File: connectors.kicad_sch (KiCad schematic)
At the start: 6 parts, among them J1 Conn_01x02, J2 Conn_01x02, J3 Conn_01x04, J4 Conn_01x04, J5 USB_C_Receptacle_USB2.0, J6 Conn_PIC_ICSP_ICD

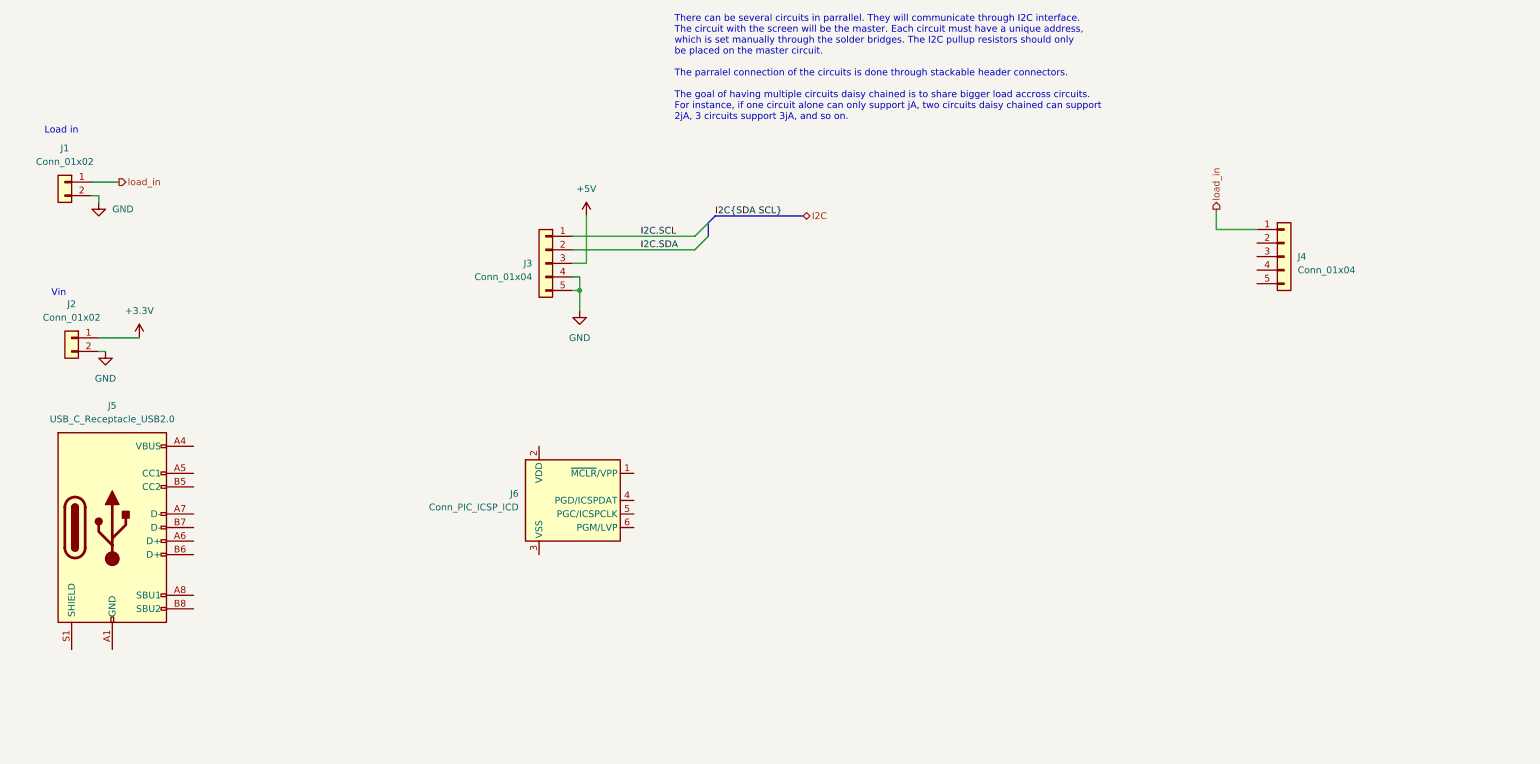
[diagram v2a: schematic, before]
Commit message: Add uart usb controller
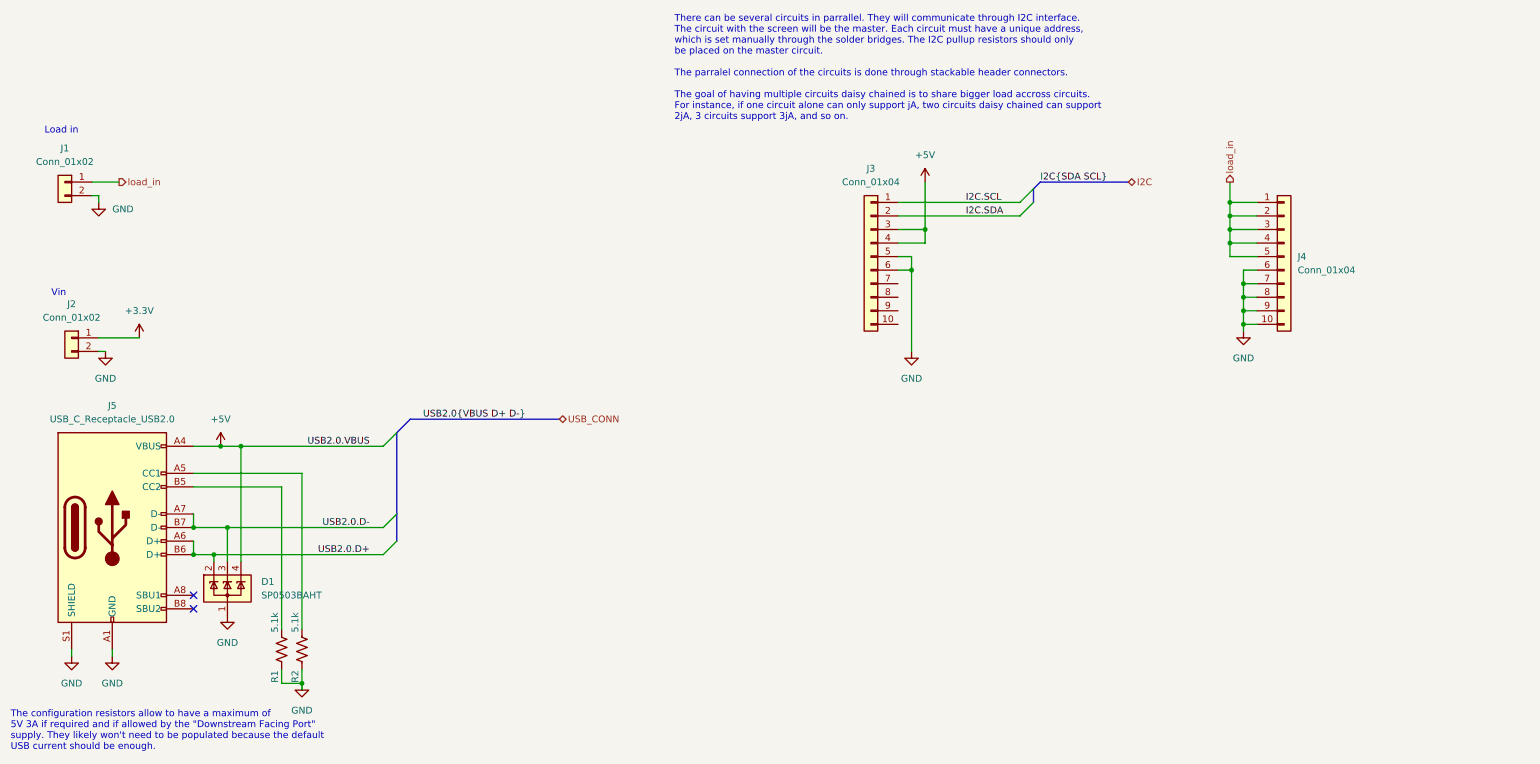
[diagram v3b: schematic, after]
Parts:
- removed J6: Conn_PIC_ICSP_ICD, Connector_PinHeader_2.54mm:PinHeader_1x06_P2.54mm_Vertical, symbol Connector:Conn_PIC_ICSP_ICD
- added D1: SP0503BAHT, Package_TO_SOT_SMD:SOT-143, symbol Power_Protection:SP0503BAHT
- added R1, R2: 5.1k, Resistor_SMD:R_0805_2012Metric, symbol Device:R_US
- J3, J4: footprint Connector_PinHeader_2.54mm:PinHeader_1x04_P2.54mm_Horizontal -> Connector_PinSocket_2.54mm:PinSocket_1x10_P2.54mm_Vertical; symbol Connector_Generic:Conn_01x05 -> Connector_Generic:Conn_01x10
- J5: footprint Connector_USB:USB_C_Plug_Molex_105444 -> Connector_USB:USB_C_Receptacle_GCT_USB4085
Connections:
- net +5V: now also J3.4 (Pin_4), J5.A4 (VBUS), J5.A9 (VBUS), J5.B4 (VBUS), J5.B9 (VBUS), D1.4 (K)
- net GND: now also J3.6 (Pin_6), J4.10 (Pin_10), J4.6 (Pin_6), J4.7 (Pin_7), J4.8 (Pin_8), J4.9 (Pin_9), J5.A1 (GND), J5.A12 (GND), J5.B1 (GND), J5.B12 (GND), J5.S1 (SHIELD), D1.1 (A), R1.1, R2.1; no longer J3.4 (Pin_4)
- net load_in: now also J4.2 (Pin_2), J4.3 (Pin_3), J4.4 (Pin_4), J4.5 (Pin_5)
- net at J5.A5 (CC1): now also R2.2
- net USB2.0.D+: now reaches J5.A6 (D+)
- net USB2.0.D+: now also J5.B6 (D+), D1.2 (K)
- net USB2.0.D-: now reaches J5.A7 (D-)
- net USB2.0.D-: now also J5.B7 (D-), D1.3 (K)
- net at J5.B5 (CC2): now also R1.2
- no-connect marks 0 -> 2
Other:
- note added: "The configuration resistors allow to have a maximum of 5V 3A if required and if allowed by the "Downstream Facing Port" supply. They likely won't need to be populated because the default USB current should be enough."

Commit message: WIP PCB Routing
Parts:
- removed J2: Conn_01x02, Connector_PinHeader_2.54mm:PinHeader_1x02_P2.54mm_Horizontal, symbol Connector_Generic:Conn_01x02
- D1: value SP0503BAHT -> (none); footprint Package_TO_SOT_SMD:SOT-143 -> (none)
- J1: value Conn_01x02 -> (none); footprint Connector_PinHeader_2.54mm:PinHeader_1x02_P2.54mm_Horizontal -> (none)
- J3, J4: value Conn_01x04 -> (none); footprint Connector_PinSocket_2.54mm:PinSocket_1x10_P2.54mm_Vertical -> (none)
- J5: value USB_C_Receptacle_USB2.0 -> (none); footprint Connector_USB:USB_C_Receptacle_GCT_USB4085 -> (none)
- R1, R2: value 5.1k -> (none); footprint Resistor_SMD:R_0805_2012Metric -> (none)
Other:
- note removed: "Vin"
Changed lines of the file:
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@@
-    (stroke (width 0) (type default) (color 0 0 0 0))
-  )
-  (wire (pts (xy 43.18 77.47) (xy 50.8 77.47))
     (stroke (width 0) (type default) (color 0 0 0 0))
   )
@@
   )
   (wire (pts (xy 60.96 113.03) (xy 67.31 113.03))
-    (stroke (width 0) (type default) (color 0 0 0 0))
-  )
-  (wire (pts (xy 43.18 80.01) (xy 44.45 80.01))
     (stroke (width 0) (type default) (color 0 0 0 0))
   )
@@
     (effects (font (size 1.27 1.27)) (justify left bottom))
   )
-  (text "Vin" (at 34.29 69.85 0)
-    (effects (font (size 1.27 1.27)) (justify left bottom))
-  )
   (text "There can be several circuits in parrallel. They will communicate through I2C interface.\nThe circuit with the screen will be the master. Each circuit must have a unique address, \nwhich is set manually through the solder bridges. The I2C pullup resistors should only \nbe placed on the master circuit.\n\nThe parralel connection of the circuits is done through stackable header connectors.\n\nThe goal of having multiple circuits daisy chained is to share bigger load accross circuits.\nFor instance, if one circuit alone can only support jA, two circuits daisy chained can support \n2jA, 3 circuits support 3jA, and so on."
     (at 151.13 36.83 0)
@@
     (in_bom yes) (on_board yes) (fields_autoplaced)
     (property "Reference" "J3" (id 0) (at 187.96 45.72 0))
-    (property "Value" "Conn_01x04" (id 1) (at 187.96 48.26 0))
-    (property "Footprint" "Connector_PinSocket_2.54mm:PinSocket_1x10_P2.54mm_Vertical" (id 2) (at 187.96 62.23 0)
+    (property "Value" "" (id 1) (at 187.96 48.26 0))
+    (property "Footprint" "" (id 2) (at 187.96 62.23 0)
       (effects (font (size 1.27 1.27)) hide)
     )
@@
     (pin "1")
   )
-  (symbol (lib_id "power:GND") (at 44.45 80.01 0) (unit 1)
-    (in_bom yes) (on_board yes) (fields_autoplaced)
-    (property "Reference" "#PWR0101" (id 0) (at 44.45 86.36 0)
-      (effects (font (size 1.27 1.27)) hide)
-    )
-    (property "Value" "GND" (id 1) (at 44.45 85.09 0))
-    (property "Footprint" "" (id 2) (at 44.45 80.01 0)
-      (effects (font (size 1.27 1.27)) hide)
-    )
-    (property "Datasheet" "" (id 3) (at 44.45 80.01 0)
-      (effects (font (size 1.27 1.27)) hide)
-    )
-    (pin "1")
-  )
   (symbol (lib_id "Device:R_US") (at 77.47 135.89 180) (unit 1)
     (in_bom no) (on_board yes)
     (property "Reference" "R1" (id 0) (at 76.2 140.97 90))
-    (property "Value" "5.1k" (id 1) (at 76.2 130.81 90))
-    (property "Footprint" "Resistor_SMD:R_0805_2012Metric" (id 2) (at 76.454 135.636 90)
+    (property "Value" "" (id 1) (at 76.2 130.81 90))
+    (property "Footprint" "" (id 2) (at 76.454 135.636 90)
       (effects (font (size 1.27 1.27)) hide)
     )
@@
     (in_bom yes) (on_board yes) (fields_autoplaced)
     (property "Reference" "J1" (id 0) (at 36.83 41.91 0))
-    (property "Value" "Conn_01x02" (id 1) (at 36.83 44.45 0))
-    (property "Footprint" "Connector_PinHeader_2.54mm:PinHeader_1x02_P2.54mm_Horizontal" (id 2) (at 36.83 48.26 0)
+    (property "Value" "" (id 1) (at 36.83 44.45 0))
+    (property "Footprint" "" (id 2) (at 36.83 48.26 0)
       (effects (font (size 1.27 1.27)) hide)
     )
@@
     (in_bom no) (on_board yes)
     (property "Reference" "R2" (id 0) (at 80.01 140.97 90))
-    (property "Value" "5.1k" (id 1) (at 80.01 130.81 90))
-    (property "Footprint" "Resistor_SMD:R_0805_2012Metric" (id 2) (at 80.264 135.636 90)
+    (property "Value" "" (id 1) (at 80.01 130.81 90))
+    (property "Footprint" "" (id 2) (at 80.264 135.636 90)
       (effects (font (size 1.27 1.27)) hide)
     )
@@
     (pin "1")
   )
-  (symbol (lib_id "Connector_Generic:Conn_01x02") (at 38.1 77.47 0) (mirror y) (unit 1)
-    (in_bom yes) (on_board yes) (fields_autoplaced)
-    (property "Reference" "J2" (id 0) (at 38.1 71.12 0))
-    (property "Value" "Conn_01x02" (id 1) (at 38.1 73.66 0))
-    (property "Footprint" "Connector_PinHeader_2.54mm:PinHeader_1x02_P2.54mm_Horizontal" (id 2) (at 38.1 77.47 0)
-      (effects (font (size 1.27 1.27)) hide)
-    )
-    (property "Datasheet" "~" (id 3) (at 38.1 77.47 0)
-      (effects (font (size 1.27 1.27)) hide)
-    )
-    (pin "1")
-    (pin "2")
-  )
-  (symbol (lib_id "power:+3.3V") (at 50.8 77.47 0) (unit 1)
-    (in_bom yes) (on_board yes) (fields_autoplaced)
-    (property "Reference" "#PWR0102" (id 0) (at 50.8 81.28 0)
-      (effects (font (size 1.27 1.27)) hide)
-    )
-    (property "Value" "+3.3V" (id 1) (at 50.8 72.39 0))
-    (property "Footprint" "" (id 2) (at 50.8 77.47 0)
-      (effects (font (size 1.27 1.27)) hide)
-    )
-    (property "Datasheet" "" (id 3) (at 50.8 77.47 0)
-      (effects (font (size 1.27 1.27)) hide)
-    )
-    (pin "1")
-  )
   (symbol (lib_id "Connector:USB_C_Receptacle_USB2.0") (at 45.72 113.03 0) (unit 1)
     (in_bom yes) (on_board yes) (fields_autoplaced)
     (property "Reference" "J5" (id 0) (at 45.72 90.17 0))
-    (property "Value" "USB_C_Receptacle_USB2.0" (id 1) (at 45.72 92.71 0))
-    (property "Footprint" "Connector_USB:USB_C_Receptacle_GCT_USB4085" (id 2) (at 49.53 113.03 0)
+    (property "Value" "" (id 1) (at 45.72 92.71 0))
+    (property "Footprint" "" (id 2) (at 49.53 113.03 0)
       (effects (font (size 1.27 1.27)) hide)
     )
@@
       (effects (font (size 1.27 1.27)) (justify left))
     )
-    (property "Value" "Conn_01x04" (id 1) (at 267.97 64.7699 0)
+    (property "Value" "" (id 1) (at 267.97 64.7699 0)
       (effects (font (size 1.27 1.27)) (justify left))
     )
-    (property "Footprint" "Connector_PinSocket_2.54mm:PinSocket_1x10_P2.54mm_Vertical" (id 2) (at 265.43 62.23 0)
+    (property "Footprint" "" (id 2) (at 265.43 62.23 0)
       (effects (font (size 1.27 1.27)) hide)
     )
@@
       (effects (font (size 1.27 1.27)) (justify left))
     )
-    (property "Value" "SP0503BAHT" (id 1) (at 73.66 125.7299 0)
+    (property "Value" "" (id 1) (at 73.66 125.7299 0)
       (effects (font (size 1.27 1.27)) (justify left))
     )
-    (property "Footprint" "Package_TO_SOT_SMD:SOT-143" (id 2) (at 73.025 125.73 0)
+    (property "Footprint" "" (id 2) (at 73.025 125.73 0)
       (effects (font (size 1.27 1.27)) (justify left) hide)
     )

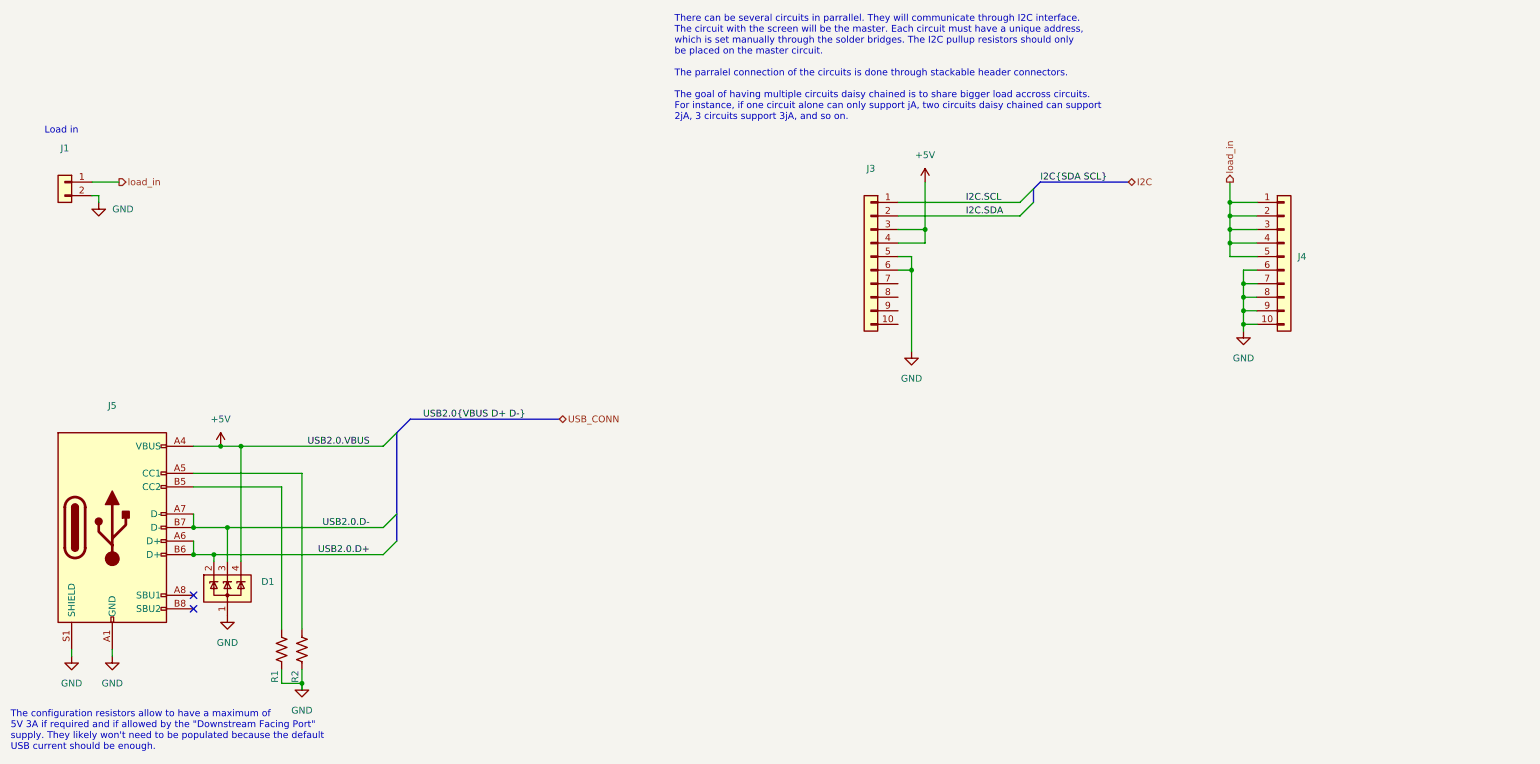
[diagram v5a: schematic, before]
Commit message: Add heatsink, among other things
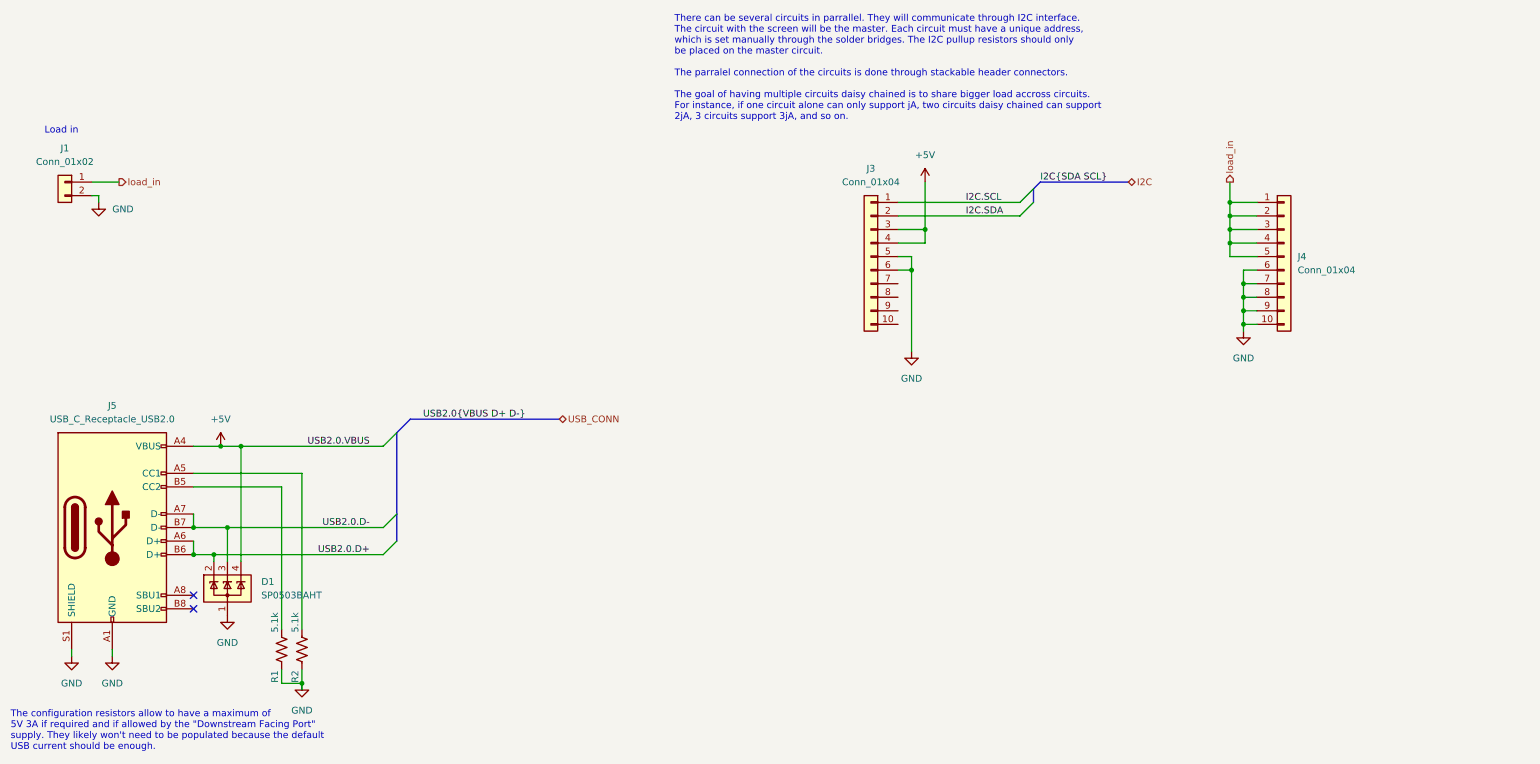
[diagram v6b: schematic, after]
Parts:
- D1: value (none) -> SP0503BAHT; footprint (none) -> Package_TO_SOT_SMD:SOT-143
- J1: value (none) -> Conn_01x02; footprint (none) -> Connector_PinHeader_2.54mm:PinHeader_1x02_P2.54mm_Horizontal
- J3, J4: value (none) -> Conn_01x04; footprint (none) -> Connector_PinSocket_2.54mm:PinSocket_1x10_P2.54mm_Vertical
- J5: value (none) -> USB_C_Receptacle_USB2.0; footprint (none) -> Connector_USB:USB_C_Receptacle_GCT_USB4085
- R1, R2: value (none) -> 5.1k; footprint (none) -> Resistor_SMD:R_0805_2012Metric
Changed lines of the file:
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@@
     (in_bom yes) (on_board yes) (fields_autoplaced)
     (property "Reference" "J3" (id 0) (at 187.96 45.72 0))
-    (property "Value" "" (id 1) (at 187.96 48.26 0))
-    (property "Footprint" "" (id 2) (at 187.96 62.23 0)
+    (property "Value" "Conn_01x04" (id 1) (at 187.96 48.26 0))
+    (property "Footprint" "Connector_PinSocket_2.54mm:PinSocket_1x10_P2.54mm_Vertical" (id 2) (at 187.96 62.23 0)
       (effects (font (size 1.27 1.27)) hide)
     )
@@
     (in_bom no) (on_board yes)
     (property "Reference" "R1" (id 0) (at 76.2 140.97 90))
-    (property "Value" "" (id 1) (at 76.2 130.81 90))
-    (property "Footprint" "" (id 2) (at 76.454 135.636 90)
+    (property "Value" "5.1k" (id 1) (at 76.2 130.81 90))
+    (property "Footprint" "Resistor_SMD:R_0805_2012Metric" (id 2) (at 76.454 135.636 90)
       (effects (font (size 1.27 1.27)) hide)
     )
@@
     (in_bom yes) (on_board yes) (fields_autoplaced)
     (property "Reference" "J1" (id 0) (at 36.83 41.91 0))
-    (property "Value" "" (id 1) (at 36.83 44.45 0))
-    (property "Footprint" "" (id 2) (at 36.83 48.26 0)
+    (property "Value" "Conn_01x02" (id 1) (at 36.83 44.45 0))
+    (property "Footprint" "Connector_PinHeader_2.54mm:PinHeader_1x02_P2.54mm_Horizontal" (id 2) (at 36.83 48.26 0)
       (effects (font (size 1.27 1.27)) hide)
     )
@@
     (in_bom no) (on_board yes)
     (property "Reference" "R2" (id 0) (at 80.01 140.97 90))
-    (property "Value" "" (id 1) (at 80.01 130.81 90))
-    (property "Footprint" "" (id 2) (at 80.264 135.636 90)
+    (property "Value" "5.1k" (id 1) (at 80.01 130.81 90))
+    (property "Footprint" "Resistor_SMD:R_0805_2012Metric" (id 2) (at 80.264 135.636 90)
       (effects (font (size 1.27 1.27)) hide)
     )
@@
     (in_bom yes) (on_board yes) (fields_autoplaced)
     (property "Reference" "J5" (id 0) (at 45.72 90.17 0))
-    (property "Value" "" (id 1) (at 45.72 92.71 0))
-    (property "Footprint" "" (id 2) (at 49.53 113.03 0)
+    (property "Value" "USB_C_Receptacle_USB2.0" (id 1) (at 45.72 92.71 0))
+    (property "Footprint" "Connector_USB:USB_C_Receptacle_GCT_USB4085" (id 2) (at 49.53 113.03 0)
       (effects (font (size 1.27 1.27)) hide)
     )
@@
       (effects (font (size 1.27 1.27)) (justify left))
     )
-    (property "Value" "" (id 1) (at 267.97 64.7699 0)
-      (effects (font (size 1.27 1.27)) (justify left))
-    )
-    (property "Footprint" "" (id 2) (at 265.43 62.23 0)
+    (property "Value" "Conn_01x04" (id 1) (at 267.97 64.7699 0)
+      (effects (font (size 1.27 1.27)) (justify left))
+    )
+    (property "Footprint" "Connector_PinSocket_2.54mm:PinSocket_1x10_P2.54mm_Vertical" (id 2) (at 265.43 62.23 0)
       (effects (font (size 1.27 1.27)) hide)
     )
@@
       (effects (font (size 1.27 1.27)) (justify left))
     )
-    (property "Value" "" (id 1) (at 73.66 125.7299 0)
-      (effects (font (size 1.27 1.27)) (justify left))
-    )
-    (property "Footprint" "" (id 2) (at 73.025 125.73 0)
+    (property "Value" "SP0503BAHT" (id 1) (at 73.66 125.7299 0)
+      (effects (font (size 1.27 1.27)) (justify left))
+    )
+    (property "Footprint" "Package_TO_SOT_SMD:SOT-143" (id 2) (at 73.025 125.73 0)
       (effects (font (size 1.27 1.27)) (justify left) hide)
     )
